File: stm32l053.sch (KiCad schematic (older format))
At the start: 5 parts, among them P1 CONN_01X25, P2 CONN_01X25, U1 STM32_LQFP64

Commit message: Power
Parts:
- added C?: 100nF, symbol C
- added C?: C, symbol C
- added R? (x2): 0, symbol R
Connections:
- net labels added: MCO, NRST, SWCLK, SWDIO, SWO
- wire segments 10 -> 25
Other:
- note added: "Absolute max of 3.6v"
- note added: "If USB is not used this\npin must be tied to VDD ."
- note added: "The VLCD pin should be connected to \nVDDA if the LCD peripheral is not used."
- moved on the sheet: C1, C2

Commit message: SWO connector
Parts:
- added P?: SWD, symbol CONN_01X06
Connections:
- wire segments 25 -> 27
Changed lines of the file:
@@
-$EndComp
-$Comp
-L VDD #PWR012
-U 1 1 58023F0F
-P 4250 1900
-F 0 "#PWR012" H 4250 1750 50  0001 C CNN
-F 1 "VDD" H 4250 2050 50  0000 C CNN
-F 2 "" H 4250 1900 50  0000 C CNN
-F 3 "" H 4250 1900 50  0000 C CNN
-	1    4250 1900
-	1    0    0    -1
 $EndComp
 $Comp
@@
 Text Notes 5200 700  0    60   ~ 12
 Absolute max of 3.6v
-Text GLabel 6500 2300 2    60   Input ~ 12
+Text GLabel 6500 2300 2    60   Input ~ 0
 SWO
 Wire Wire Line
 	6500 2300 6200 2300
-Text GLabel 3750 3400 0    60   Input ~ 12
+Text GLabel 4150 3400 0    60   Input ~ 0
 SWCLK
-Text GLabel 4150 3300 0    60   Input ~ 12
+Text GLabel 4150 3300 0    60   Input ~ 0
 SWDIO
 Wire Wire Line
 	4250 3300 4150 3300
 Wire Wire Line
-	3750 3400 4250 3400
-Text GLabel 6550 4200 2    60   Input ~ 12
+	4150 3400 4250 3400
+Text GLabel 6550 4200 2    60   Input ~ 0
 NRST
 Wire Wire Line
 	6550 4200 6200 4200
-Text GLabel 6550 4850 2    60   Input ~ 12
+Text GLabel 6550 4850 2    60   Input ~ 0
 MCO
 Wire Wire Line
@@
 Wire Wire Line
 	6500 4950 6200 4950
+Wire Wire Line
+	6200 4300 6200 4400
+$Comp
+L CONN_01X06 P?
+U 1 1 58036840
+P 1550 1800
+F 0 "P?" H 1550 2150 50  0000 C CNN
+F 1 "SWD" V 1650 1800 50  0000 C CNN
+F 2 "" H 1550 1800 50  0000 C CNN
+F 3 "" H 1550 1800 50  0000 C CNN
+	1    1550 1800
+	-1   0    0    -1
+$EndComp
+$Comp
+L Earth #PWR?
+U 1 1 580369A9
+P 2250 1750
+F 0 "#PWR?" H 2250 1500 50  0001 C CNN
+F 1 "Earth" H 2250 1600 50  0001 C CNN
+F 2 "" H 2250 1750 50  0000 C CNN
+F 3 "" H 2250 1750 50  0000 C CNN
+	1    2250 1750
+	1    0    0    -1
+$EndComp
+Wire Wire Line
+	2250 1750 1750 1750
+Text GLabel 1750 1650 2    60   Input ~ 0
+SWCLK
+Text GLabel 1750 1850 2    60   Input ~ 0
+SWDIO
+Text GLabel 1750 1950 2    60   Input ~ 0
+NRST
+Text GLabel 1750 2050 2    60   Input ~ 0
+SWO
+$Comp
+L VDD #PWR?
+U 1 1 5803734F
+P 1750 1550
+F 0 "#PWR?" H 1750 1400 50  0001 C CNN
+F 1 "VDD" H 1750 1700 50  0000 C CNN
+F 2 "" H 1750 1550 50  0000 C CNN
+F 3 "" H 1750 1550 50  0000 C CNN
+	1    1750 1550
+	1    0    0    -1
+$EndComp
 $EndSCHEMATC

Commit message: PA header
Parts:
- removed C2: 100nF, Capacitors_SMD:C_0805_HandSoldering, symbol C
- removed P1, P2: CONN_01X25, Pin_Headers:Pin_Header_Straight_1x25, symbol CONN_01X25
- added P?: Ext Xtal, symbol CONN_01X02
- added P?: PA, symbol CONN_01X14
- added R?: 10K, symbol R
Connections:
- net labels added: BOOT0, OSC32_IN, OSC32_OUT, PA0, PA1, PA10, PA11, PA12, PA15, PA2, PA3, PA4, PA5, PA6, PA7, PA8, PA9
- net labels removed: VDDA
- wire segments 27 -> 52
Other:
- moved on the sheet: C1, C?, R?, U1

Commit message: PB header
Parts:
- added P?: CN_PB, symbol CONN_01X15
- P?: value PA -> CN_PA
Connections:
- net PB0: now reaches U1.26 (PB0)
- net PB0: now also P?.1 (P1)
- net PB1: now reaches U1.27 (PB1)
- net PB1: now also P?.2 (P2)
- net PB2: now reaches U1.28 (PB2)
- net PB2: now also P?.3 (P3)
- net PB10: now reaches U1.29 (PB10)
- net PB10: now also P?.10 (P10)
- net PB11: now reaches U1.30 (PB11)
- net PB11: now also P?.11 (P11)
- net PB12: now reaches U1.33 (PB12)
- net PB12: now also P?.12 (P12)
- net PB13: now reaches U1.34 (PB13)
- net PB13: now also P?.13 (P13)
- net PB14: now reaches U1.35 (PB14)
- net PB14: now also P?.14 (P14)
- net PB15: now reaches U1.36 (PB15)
- net PB15: now also P?.15 (P15)
- net PB4: now reaches U1.56 (PB4)
- net PB4: now also P?.4 (P4)
- net PB5: now reaches U1.57 (PB5)
- net PB5: now also P?.5 (P5)
- net PB6: now reaches U1.58 (PB6)
- net PB6: now also P?.6 (P6)
- net PB7: now reaches U1.59 (PB7)
- net PB7: now also P?.7 (P7)
- net PB8: now reaches U1.61 (PB8)
- net PB8: now also P?.8 (P8)
- net PB9: now reaches U1.62 (PB9)
- net PB9: now also P?.9 (P9)
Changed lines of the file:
@@
 Text Notes 7450 900  0    60   ~ 12
 Absolute max of 3.6v
-Text GLabel 8450 2500 2    60   Input ~ 0
+Text GLabel 8950 2500 2    60   Input ~ 0
 SWO
 Text GLabel 6150 3600 0    60   Input ~ 0
@@
 P 1700 3150
 F 0 "P?" H 1700 3900 50  0000 C CNN
-F 1 "PA" V 1800 3150 50  0000 C CNN
+F 1 "CN_PA" V 1800 3150 50  0000 C CNN
 F 2 "" H 1700 3150 50  0000 C CNN
 F 3 "" H 1700 3150 50  0000 C CNN
@@
 Wire Wire Line
 	1200 3800 1500 3800
+Text Label 8800 2200 2    60   ~ 0
+PB0
+Text Label 8800 2300 2    60   ~ 0
+PB1
+Text Label 8800 2400 2    60   ~ 0
+PB2
+Wire Wire Line
+	8450 2200 8800 2200
+Wire Wire Line
+	8450 2300 8800 2300
+Wire Wire Line
+	8450 2400 8800 2400
+Text Label 8800 2600 2    60   ~ 0
+PB4
+Text Label 8800 2700 2    60   ~ 0
+PB5
+Text Label 8800 2800 2    60   ~ 0
+PB6
+Text Label 8800 2900 2    60   ~ 0
+PB7
+Text Label 8800 3000 2    60   ~ 0
+PB8
+Wire Wire Line
+	8450 2500 8950 2500
+Wire Wire Line
+	8450 2600 8800 2600
+Wire Wire Line
+	8450 2700 8800 2700
+Wire Wire Line
+	8450 2800 8800 2800
+Wire Wire Line
+	8450 2900 8800 2900
+Wire Wire Line
+	8800 3000 8450 3000
+Text Label 8800 3100 2    60   ~ 0
+PB9
+Text Label 8800 3200 2    60   ~ 0
+PB10
+Text Label 8800 3300 2    60   ~ 0
+PB11
+Text Label 8800 3400 2    60   ~ 0
+PB12
+Text Label 8800 3500 2    60   ~ 0
+PB13
+Text Label 8800 3600 2    60   ~ 0
+PB14
+Text Label 8800 3700 2    60   ~ 0
+PB15
+Wire Wire Line
+	8450 3100 8800 3100
+Wire Wire Line
+	8450 3200 8800 3200
+Wire Wire Line
+	8450 3300 8800 3300
+Wire Wire Line
+	8450 3400 8800 3400
+Wire Wire Line
+	8450 3500 8800 3500
+Wire Wire Line
+	8450 3600 8800 3600
+Wire Wire Line
+	8450 3700 8800 3700
+$Comp
+L CONN_01X15 P?
+U 1 1 5803B06C
+P 2450 3200
+F 0 "P?" H 2450 4000 50  0000 C CNN
+F 1 "CN_PB" V 2550 3200 50  0000 C CNN
+F 2 "" H 2450 3200 50  0000 C CNN
+F 3 "" H 2450 3200 50  0000 C CNN
+	1    2450 3200
+	-1   0    0    -1
+$EndComp
+Text Label 3000 2500 2    60   ~ 0
+PB0
+Text Label 3000 2600 2    60   ~ 0
+PB1
+Text Label 3000 2700 2    60   ~ 0
+PB2
+Wire Wire Line
+	2650 2500 3000 2500
+Wire Wire Line
+	2650 2600 3000 2600
+Wire Wire Line
+	2650 2700 3000 2700
+Text Label 3000 2800 2    60   ~ 0
+PB4
+Text Label 3000 2900 2    60   ~ 0
+PB5
+Text Label 3000 3000 2    60   ~ 0
+PB6
+Text Label 3000 3100 2    60   ~ 0
+PB7
+Text Label 3000 3200 2    60   ~ 0
+PB8
+Wire Wire Line
+	2650 2800 3000 2800
+Wire Wire Line
+	2650 2900 3000 2900
+Wire Wire Line
+	2650 3000 3000 3000
+Wire Wire Line
+	2650 3100 3000 3100
+Wire Wire Line
+	3000 3200 2650 3200
+Text Label 3000 3300 2    60   ~ 0
+PB9
+Text Label 3000 3400 2    60   ~ 0
+PB10
+Text Label 3000 3500 2    60   ~ 0
+PB11
+Text Label 3000 3600 2    60   ~ 0
+PB12
+Text Label 3000 3700 2    60   ~ 0
+PB13
+Text Label 3000 3800 2    60   ~ 0
+PB14
+Text Label 3000 3900 2    60   ~ 0
+PB15
+Wire Wire Line
+	2650 3300 3000 3300
+Wire Wire Line
+	2650 3400 3000 3400
+Wire Wire Line
+	2650 3500 3000 3500
+Wire Wire Line
+	2650 3600 3000 3600
+Wire Wire Line
+	2650 3700 3000 3700
+Wire Wire Line
+	2650 3800 3000 3800
+Wire Wire Line
+	2650 3900 3000 3900
 $EndSCHEMATC

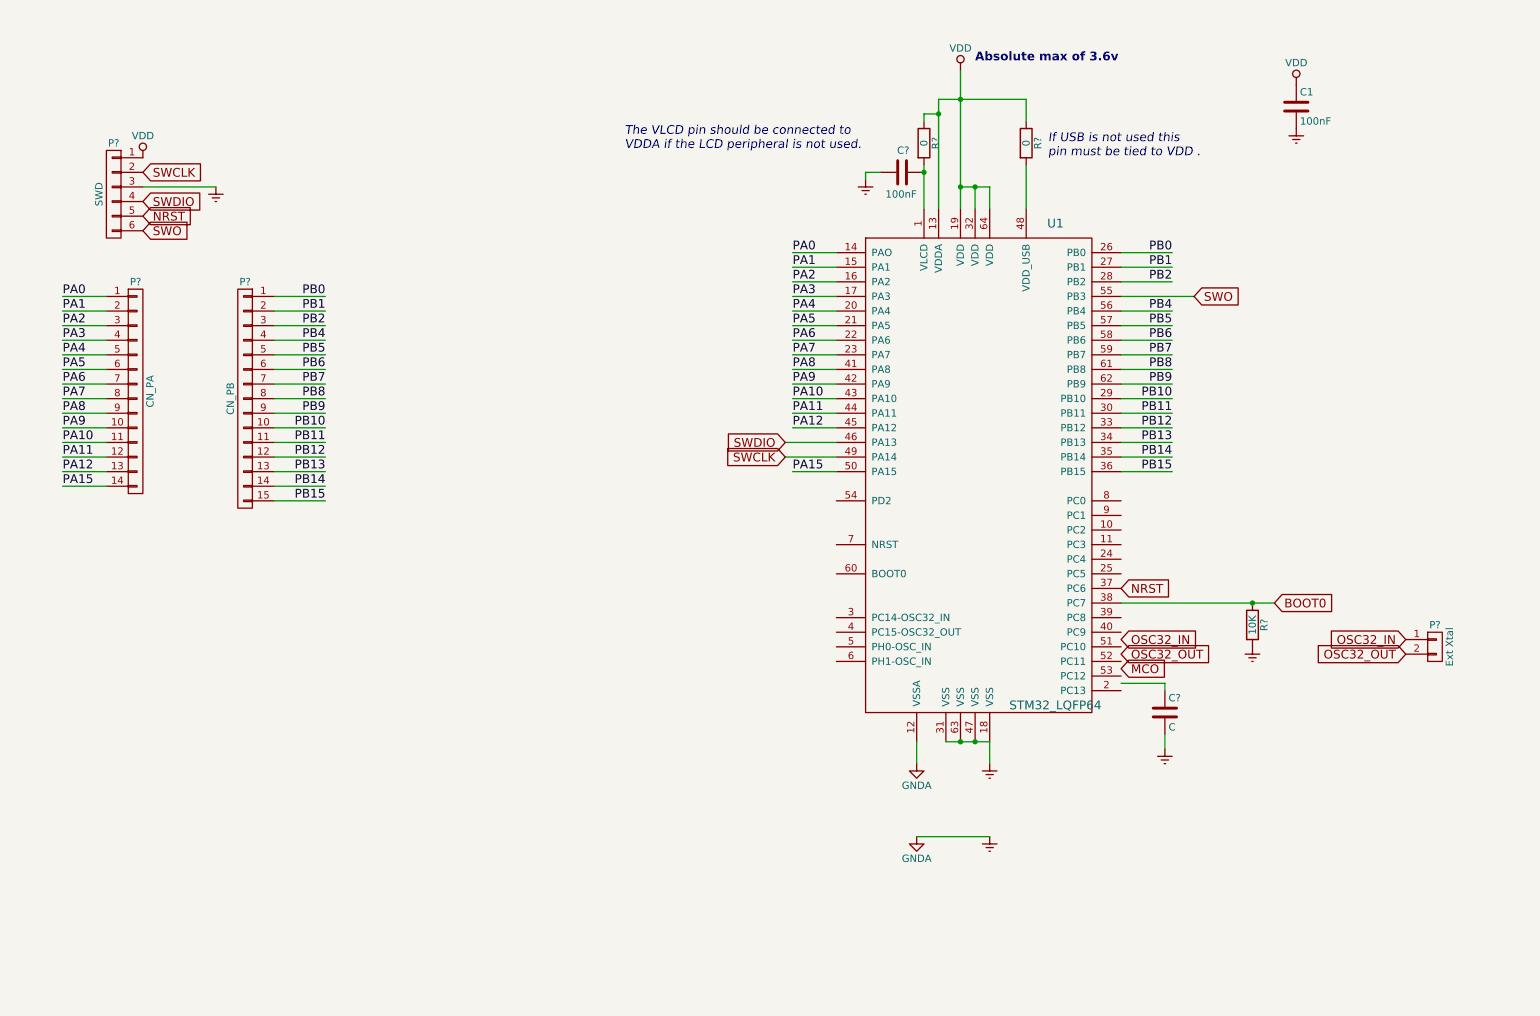
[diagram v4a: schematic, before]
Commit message: 23 pin headers
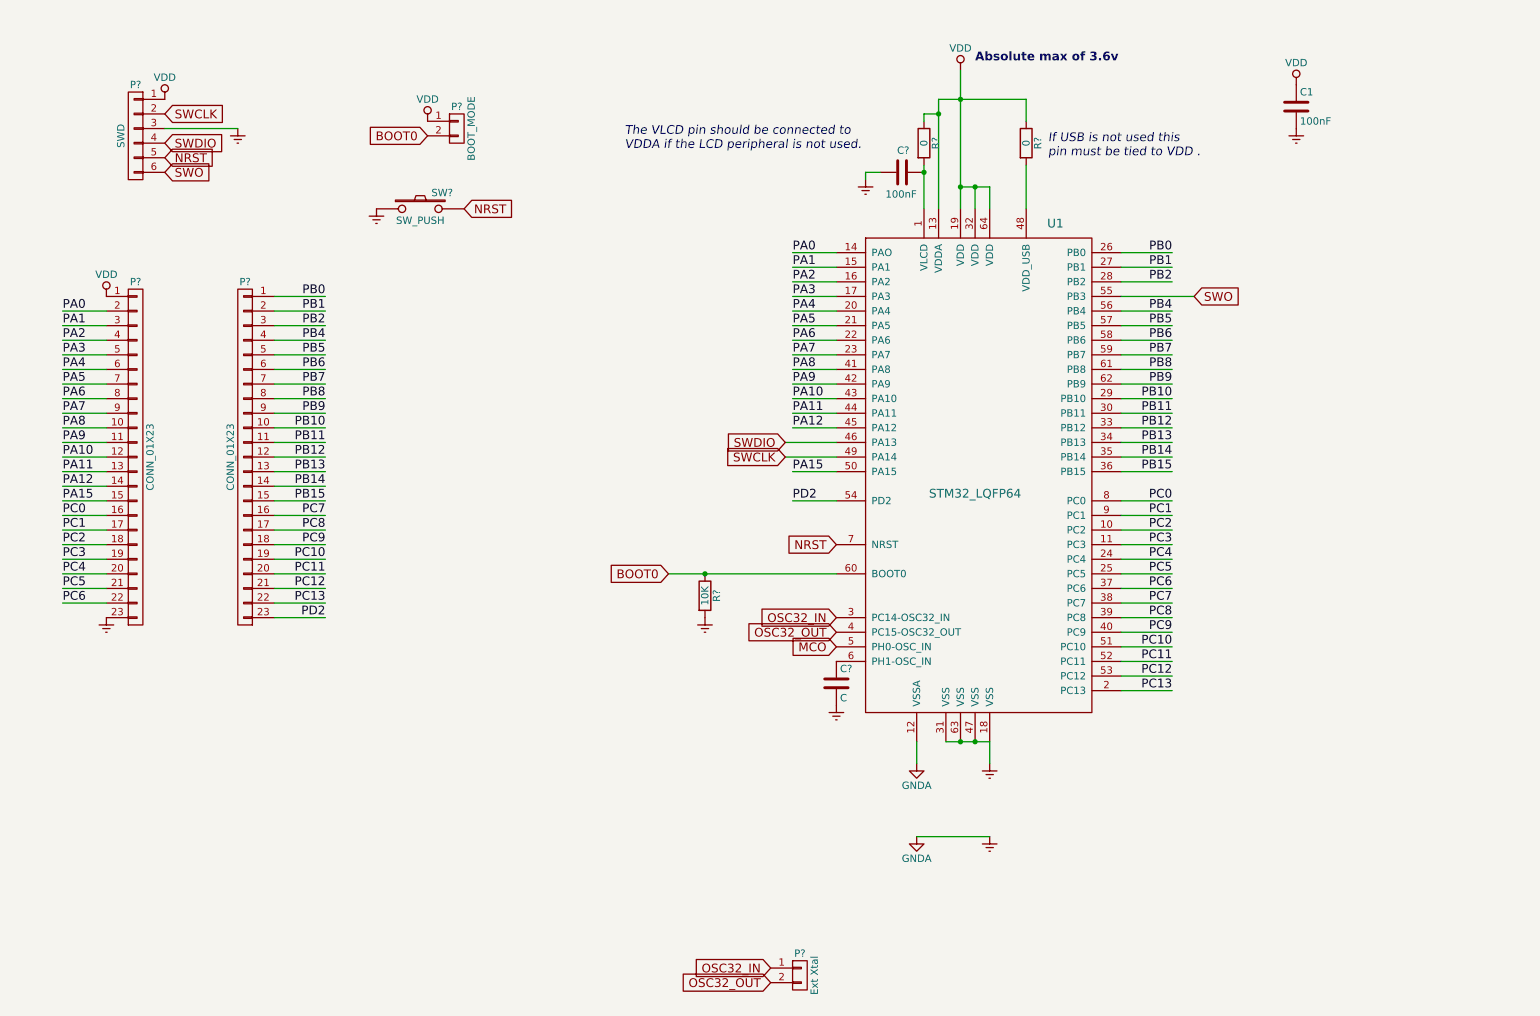
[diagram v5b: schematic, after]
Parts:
- removed P?: CN_PA, symbol CONN_01X14
- removed P?: CN_PB, symbol CONN_01X15
- added P? (x2): CONN_01X23, symbol CONN_01X23
- added P?: BOOT_MODE, symbol CONN_01X02
- added SW?: SW_PUSH, symbol SW_PUSH
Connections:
- net BOOT0: now also U1.60 (BOOT0), P?.2 (P2); no longer U1.38 (PC7)
- net Earth: now also P?.23 (P23), SW?.1
- net MCO: now also U1.5 (PH0-OSC_IN)
- net NRST: now also U1.7 (NRST), SW?.2; no longer U1.37 (PC6)
- net OSC32_IN: now also U1.3 (PC14-OSC32_IN)
- net OSC32_OUT: now also U1.4 (PC15-OSC32_OUT)
- net PA0: now also P?.2 (P2)
- net PA1: now also P?.3 (P3)
- net PA10: now also P?.12 (P12)
- net PA11: now also P?.13 (P13)
- net PA12: now also P?.14 (P14)
- net PA15: now also P?.15 (P15)
- net PA2: now also P?.4 (P4)
- net PA3: now also P?.5 (P5)
- net PA4: now also P?.6 (P6)
- net PA5: now also P?.7 (P7)
- net PA6: now also P?.8 (P8)
- net PA7: now also P?.9 (P9)
- net PA8: now also P?.10 (P10)
- net PA9: now also P?.11 (P11)
- net PB0: now also P?.1 (P1)
- net PB1: now also P?.2 (P2)
- net PB10: now also P?.10 (P10)
- net PB11: now also P?.11 (P11)
- net PB12: now also P?.12 (P12)
- net PB13: now also P?.13 (P13)
- net PB14: now also P?.14 (P14)
- net PB15: now also P?.15 (P15)
- net PB2: now also P?.3 (P3)
- net PB4: now also P?.4 (P4)
- net PB5: now also P?.5 (P5)
- net PB6: now also P?.6 (P6)
- net PB7: now also P?.7 (P7)
- net PB8: now also P?.8 (P8)
- net PB9: now also P?.9 (P9)
- net VDD: now also P?.1 (P1), P?.1 (P1)
- net PC2: now reaches U1.10 (PC2)
- net PC2: now also P?.18 (P18)
- net PC3: now reaches U1.11 (PC3)
- net PC3: now also P?.19 (P19)
- net PC13: now reaches U1.2 (PC13)
- net PC13: now also P?.22 (P22)
- net PC4: now reaches U1.24 (PC4)
- net PC4: now also P?.20 (P20)
- net PC5: now reaches U1.25 (PC5)
- net PC5: now also P?.21 (P21)
- net PC8: now reaches U1.39 (PC8)
- net PC8: now also P?.17 (P17)
- net PC9: now reaches U1.40 (PC9)
- net PC9: now also P?.18 (P18)
- net PC10: now reaches U1.51 (PC10)
- net PC10: now also P?.19 (P19)
- net PC11: now reaches U1.52 (PC11)
- net PC11: now also P?.20 (P20)
- net PC12: now reaches U1.53 (PC12)
- net PC12: now also P?.21 (P21)
- net PD2: now reaches U1.54 (PD2)
- net PD2: now also P?.23 (P23)
- net at U1.6 (PH1-OSC_IN): now also C?.1
- net PC0: now reaches U1.8 (PC0)
- net PC0: now also P?.16 (P16)
- net PC1: now reaches U1.9 (PC1)
- net PC1: now also P?.17 (P17)
- new net PC6: P?.22 (P22), U1.37 (PC6)
- new net PC7: P?.16 (P16), U1.38 (PC7)
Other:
- moved on the sheet: C?, P?, R?
